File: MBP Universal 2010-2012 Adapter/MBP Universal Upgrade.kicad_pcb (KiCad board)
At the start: 2 copper layers, 18 x 38 mm, 4 parts, among them J1 501745-0301

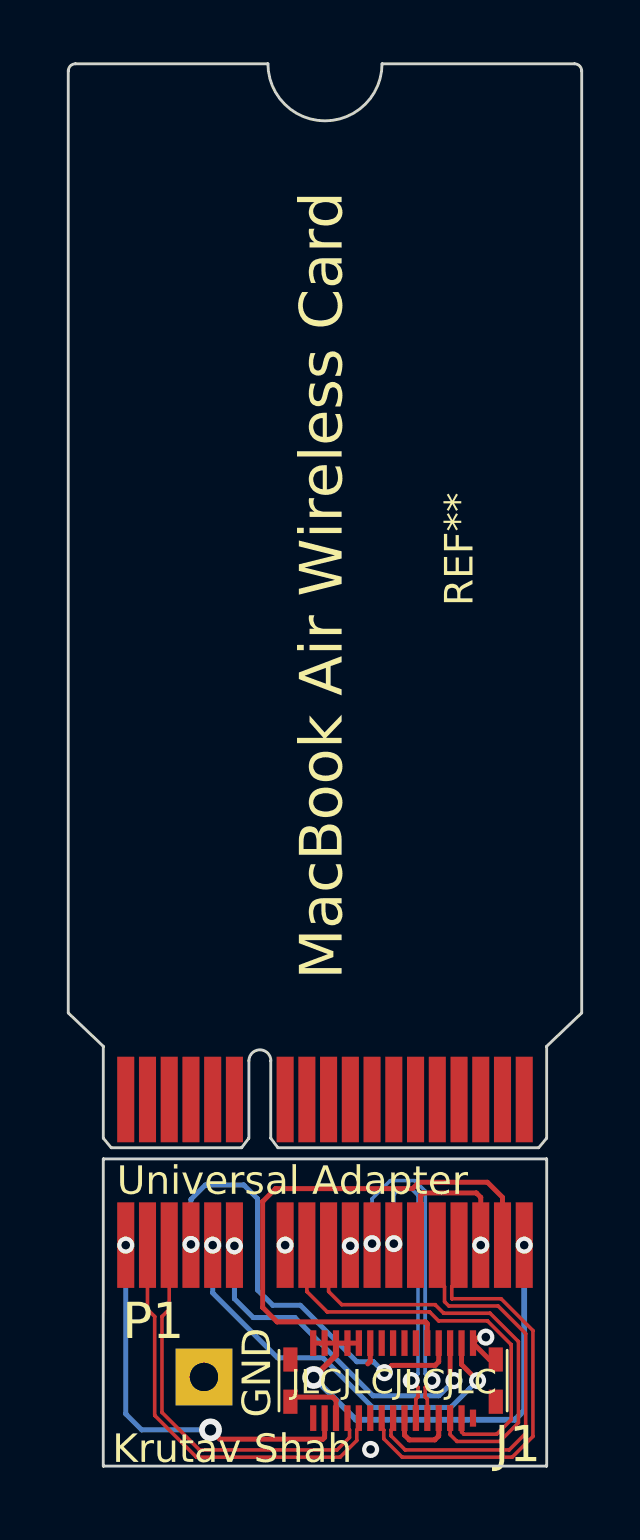
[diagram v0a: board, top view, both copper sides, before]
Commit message: Release prototype for Universal part ready.
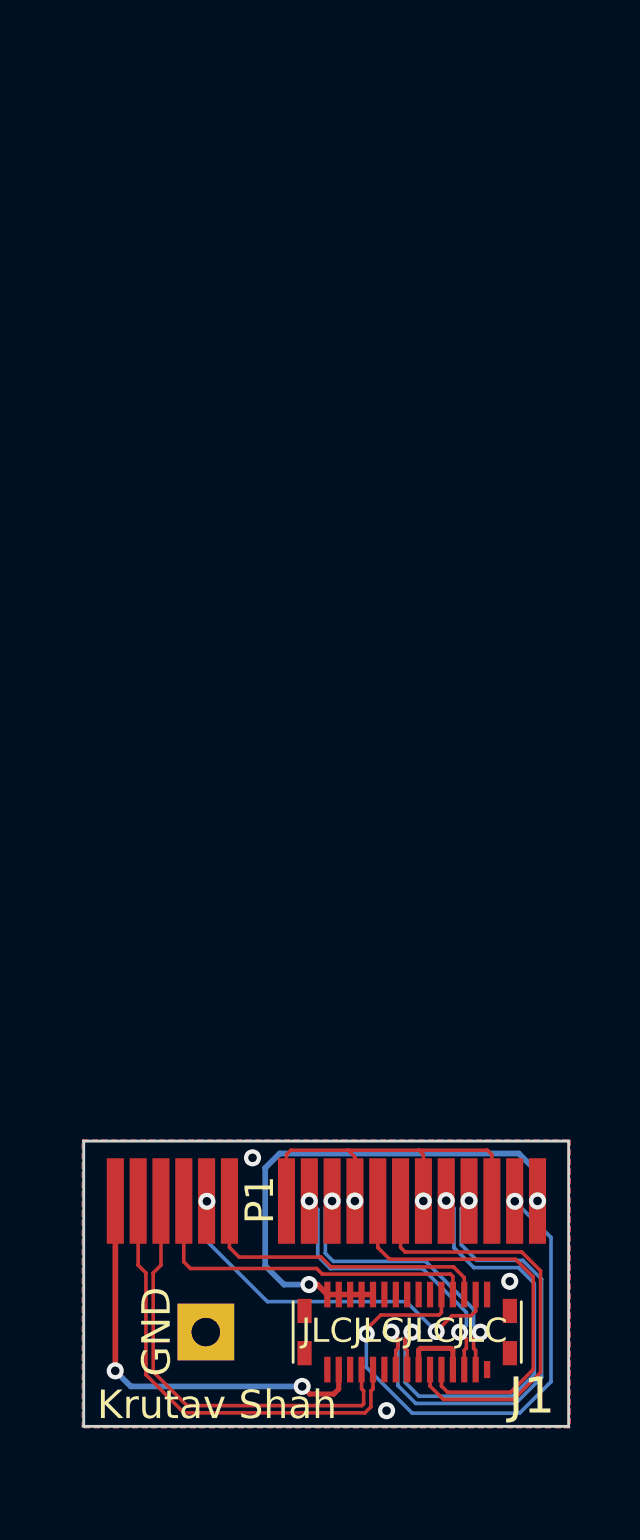
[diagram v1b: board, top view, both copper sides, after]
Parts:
- removed REF**: MacBook Air Wireless Card, MBPWirelessUpgrade:MacBook Air Wireless Card
- P1: value (none) -> Edge Connector; footprint (none) -> MBPWirelessUpgrade:Edge Connector
- moved P1 4.59 mm to (109.1, 84.1)
- moved J1 1.77 mm to (111.3, 91.9)
- moved MH2 1.58 mm to (104.3, 91.7)
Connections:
- P1 pad 10: PCIE_AP_D2R_N -> PCIE_AP_D2R_P
- P1 pad 11: PCIE_AP_D2R_P -> PCIE_AP_D2R_N
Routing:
- net PCIE_AP_D2R_N: track 15.2 -> 10.3 mm, vias 0 -> 2
- net PCIE_CLK100M_AP_N: track 10.8 -> 15.5 mm, vias 2 -> 0
- net PCIE_AP_D2R_P: track 14.7 -> 10.3 mm, vias 0 -> 2
- net GND: track 12.9 -> 16.9 mm
- net AP_CLKREQ_Q_L: track 15.9 -> 12.4 mm, vias 2 -> 0
- net PCIE_CLK100M_AP_P: track 12.0 -> 15.0 mm, vias 2 -> 0
- net PCIE_AP_R2D_N: track 15.6 -> 17.5 mm, vias 0 -> 2
- net PCIE_AP_R2D_P: track 14.7 -> 16.6 mm, vias 0 -> 2
- net WIFI_EVENT_L: track 21.0 -> 19.3 mm, vias 0 -> 2
- net AP_PCIE_WAKE_L: track 12.6 -> 10.9 mm, vias 2 -> 0
- net AP_RESET_CONN_L: track 14.6 -> 13.0 mm
- net PP3V3_WLAN: track 17.1 -> 18.7 mm
- net USB_BT_P: track 14.8 -> 16.1 mm
- net USB_BT_N: track 14.0 -> 15.2 mm
- net PP3V3_S3_BT_F: track 14.0 -> 14.9 mm
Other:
- board size 18 x 38 mm -> 17 x 10 mm

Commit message: Added pre-release fabrication files
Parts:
- renumbered MH2 to MH1
